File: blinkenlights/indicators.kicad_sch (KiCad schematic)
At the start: 50 parts, among them U401 74HC244, U402 74AUC2G34

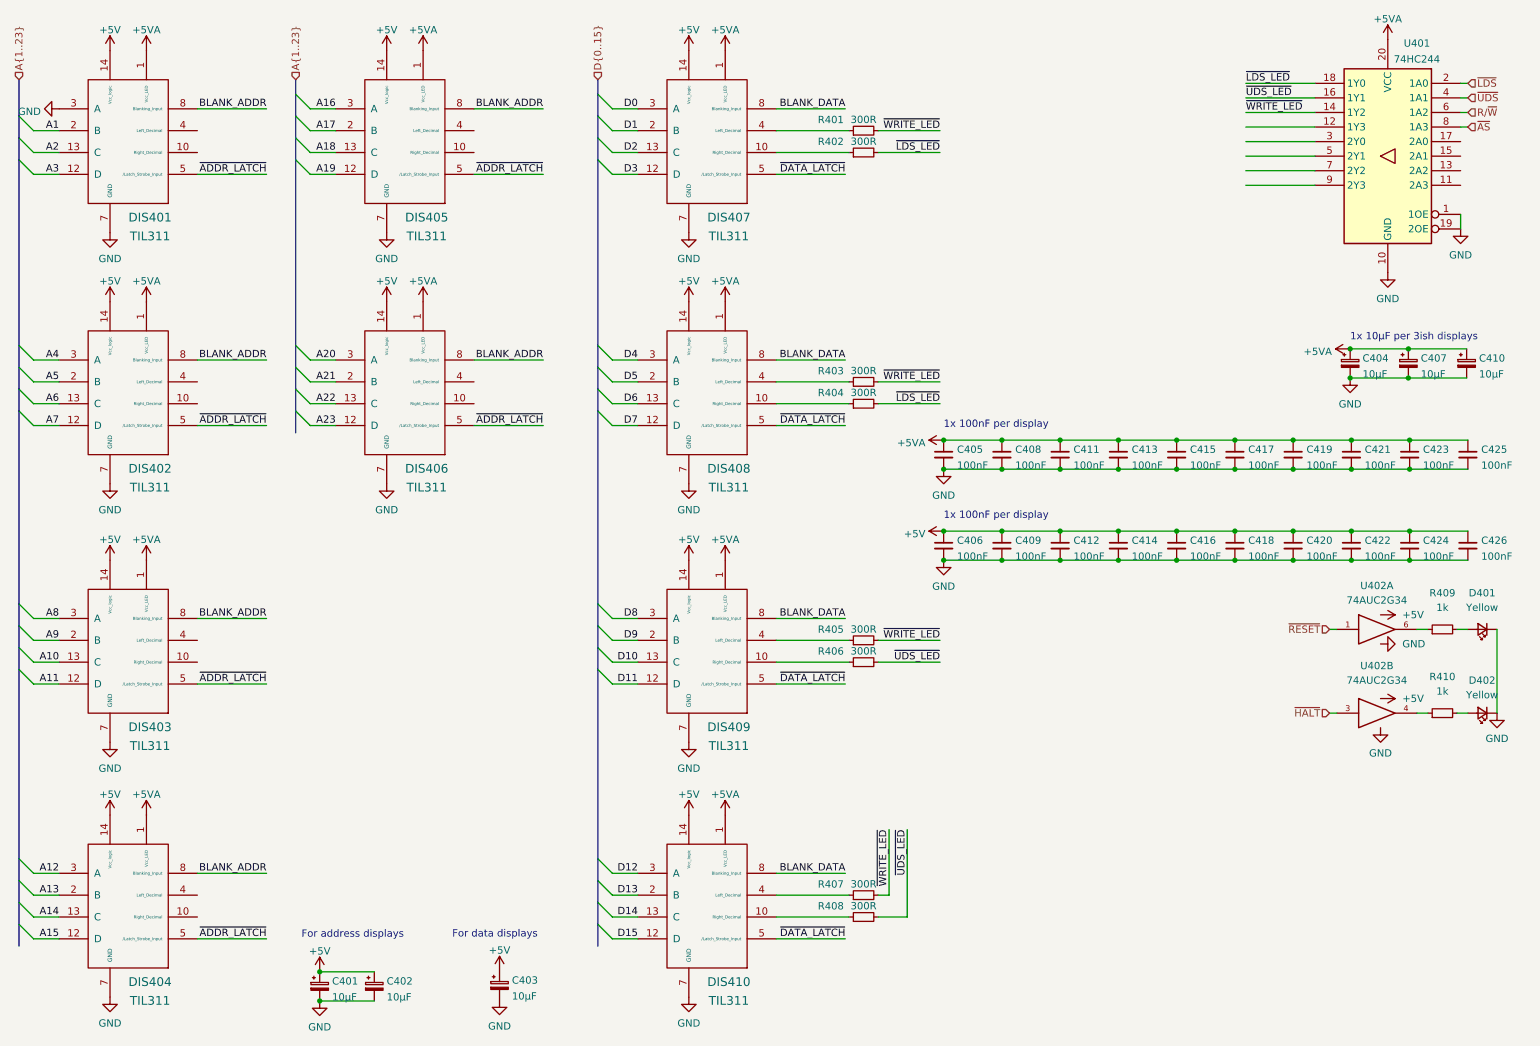
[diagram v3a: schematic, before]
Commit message: Routed address/data bus on blinkenlights
- It goes to the funky hex display bois now and is routed so that it
  should be pretty ez to yeet on down into level shifters for the big
  ARM chip that runs the show
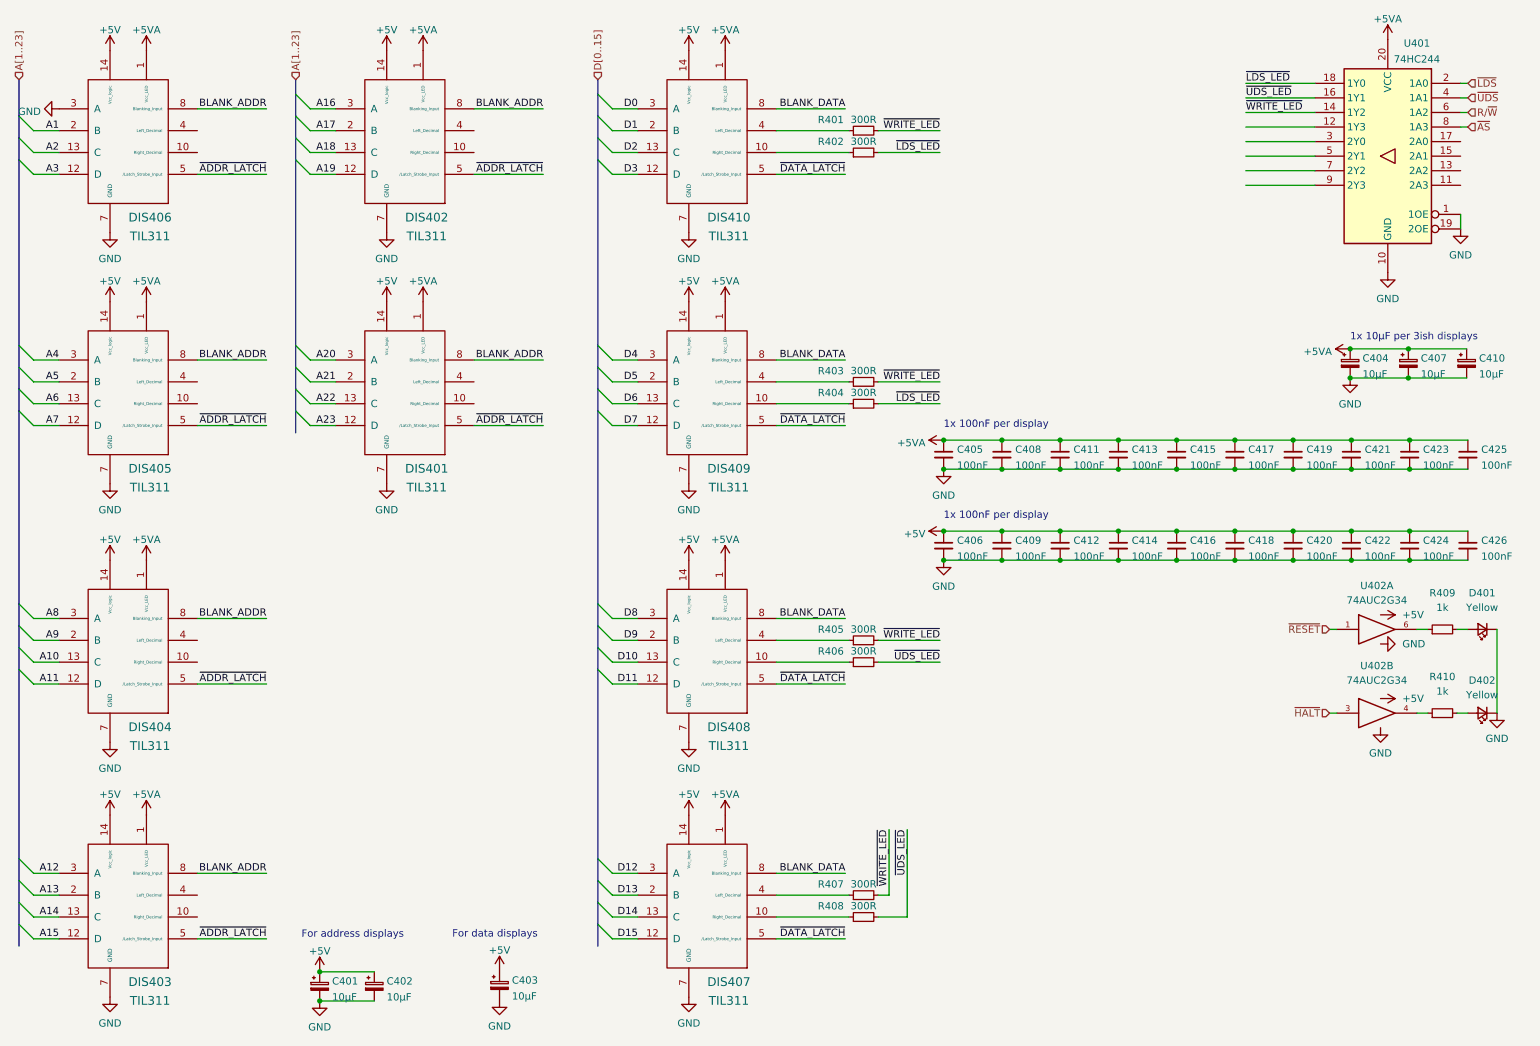
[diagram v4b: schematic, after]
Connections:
- net A1: now also DIS406.2 (B); no longer DIS401.2 (B)
- net A10: now also DIS404.13 (C); no longer DIS403.13 (C)
- net A11: now also DIS404.12 (D); no longer DIS403.12 (D)
- net A12: now also DIS403.3 (A); no longer DIS404.3 (A)
- net A13: now also DIS403.2 (B); no longer DIS404.2 (B)
- net A14: now also DIS403.13 (C); no longer DIS404.13 (C)
- net A15: now also DIS403.12 (D); no longer DIS404.12 (D)
- net A16: now also DIS402.3 (A); no longer DIS405.3 (A)
- net A17: now also DIS402.2 (B); no longer DIS405.2 (B)
- net A18: now also DIS402.13 (C); no longer DIS405.13 (C)
- net A19: now also DIS402.12 (D); no longer DIS405.12 (D)
- net A2: now also DIS406.13 (C); no longer DIS401.13 (C)
- net A20: now also DIS401.3 (A); no longer DIS406.3 (A)
- net A21: now also DIS401.2 (B); no longer DIS406.2 (B)
- net A22: now also DIS401.13 (C); no longer DIS406.13 (C)
- net A23: now also DIS401.12 (D); no longer DIS406.12 (D)
- net A3: now also DIS406.12 (D); no longer DIS401.12 (D)
- net A4: now also DIS405.3 (A); no longer DIS402.3 (A)
- net A5: now also DIS405.2 (B); no longer DIS402.2 (B)
- net A6: now also DIS405.13 (C); no longer DIS402.13 (C)
- net A7: now also DIS405.12 (D); no longer DIS402.12 (D)
- net A8: now also DIS404.3 (A); no longer DIS403.3 (A)
- net A9: now also DIS404.2 (B); no longer DIS403.2 (B)
- net D0: now also DIS410.3 (A); no longer DIS407.3 (A)
- net D1: now also DIS410.2 (B); no longer DIS407.2 (B)
- net D10: now also DIS408.13 (C); no longer DIS409.13 (C)
- net D11: now also DIS408.12 (D); no longer DIS409.12 (D)
- net D12: now also DIS407.3 (A); no longer DIS410.3 (A)
- net D13: now also DIS407.2 (B); no longer DIS410.2 (B)
- net D14: now also DIS407.13 (C); no longer DIS410.13 (C)
- net D15: now also DIS407.12 (D); no longer DIS410.12 (D)
- net D2: now also DIS410.13 (C); no longer DIS407.13 (C)
- net D3: now also DIS410.12 (D); no longer DIS407.12 (D)
- net D4: now also DIS409.3 (A); no longer DIS408.3 (A)
- net D5: now also DIS409.2 (B); no longer DIS408.2 (B)
- net D6: now also DIS409.13 (C); no longer DIS408.13 (C)
- net D7: now also DIS409.12 (D); no longer DIS408.12 (D)
- net D8: now also DIS408.3 (A); no longer DIS409.3 (A)
- net D9: now also DIS408.2 (B); no longer DIS409.2 (B)
- net GND: now also DIS406.3 (A); no longer DIS401.3 (A)
- net at DIS407.10 (Right_Decimal): now also R408.1; no longer R402.1
- net at DIS407.4 (Left_Decimal): now also R407.1; no longer R401.1
- net at DIS410.4 (Left_Decimal): now also R401.1; no longer R407.1
- net at DIS410.10 (Right_Decimal): now also R402.1; no longer R408.1
- net at R406.1: now also DIS408.10 (Right_Decimal); no longer DIS409.10 (Right_Decimal)
- net at R403.1: now also DIS409.4 (Left_Decimal); no longer DIS408.4 (Left_Decimal)
- net at R405.1: now also DIS408.4 (Left_Decimal); no longer DIS409.4 (Left_Decimal)
- net at R404.1: now also DIS409.10 (Right_Decimal); no longer DIS408.10 (Right_Decimal)
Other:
- moved on the sheet: DIS401, DIS402, DIS403, DIS404, DIS405, DIS406, DIS407, DIS408, DIS409, DIS410

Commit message: Routed control signals
- The blinkenlights board now has the control signals routed to IO
  expanders, and removed a bunch of superfluous level shifting type
  stuff
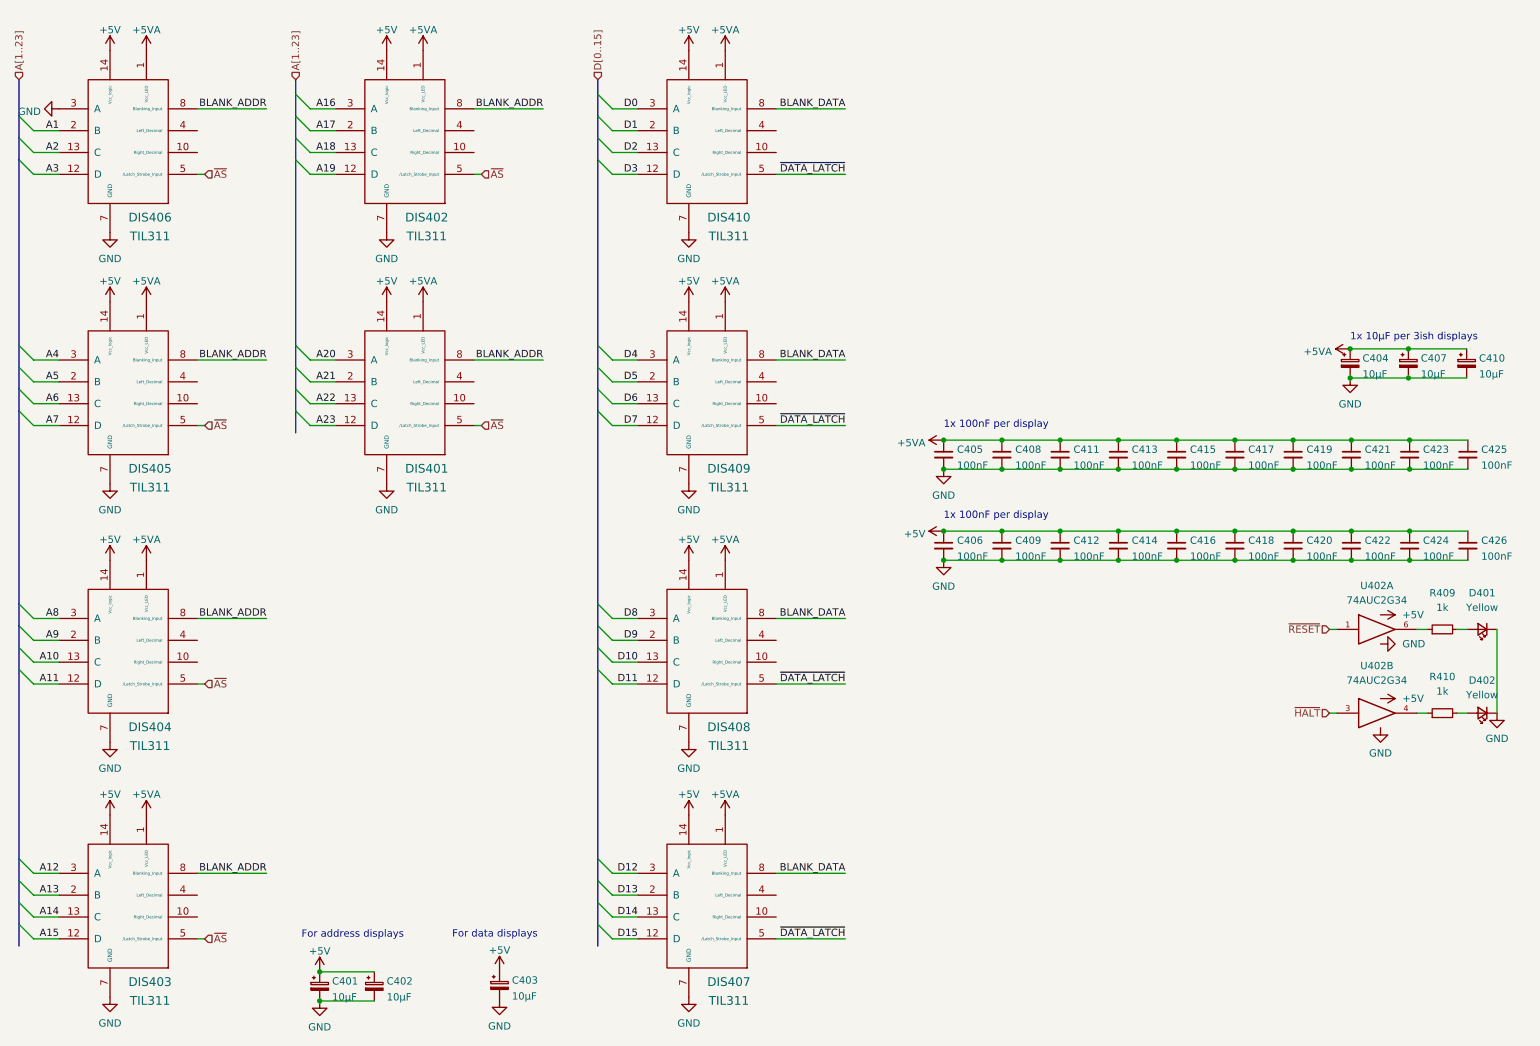
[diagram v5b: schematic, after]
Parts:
- removed R401, R402, R403, R404, R405, R406, R407, R408: 300R, Resistor_SMD:R_0805_2012Metric, symbol Device:R_Small
- removed U401: 74HC244, Package_SO:TSSOP-20_4.4x6.5mm_P0.65mm, symbol 74xx:74HC244
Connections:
- net ~{ADDR_LATCH} is gone; now on net ~{AS}: DIS401.5 (/Latch_Strobe_Input), DIS402.5 (/Latch_Strobe_Input), DIS403.5 (/Latch_Strobe_Input), DIS404.5 (/Latch_Strobe_Input), DIS405.5 (/Latch_Strobe_Input), DIS406.5 (/Latch_Strobe_Input)

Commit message: Finish routing of blinkenlights board
- Completed routing of the board, including the function code lines and
  other such fun stuff
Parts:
- U402: footprint Package_TO_SOT_SMD:SOT-23-6 -> Package_TO_SOT_SMD:SOT-23-6_Handsoldering
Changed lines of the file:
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@@
     (property "Reference" "U402" (id 0) (at 257.175 115.57 0))
     (property "Value" "74AUC2G34" (id 1) (at 257.175 118.11 0))
-    (property "Footprint" "Package_TO_SOT_SMD:SOT-23-6" (id 2) (at 257.81 123.19 0)
+    (property "Footprint" "Package_TO_SOT_SMD:SOT-23-6_Handsoldering" (id 2) (at 257.81 123.19 0)
       (effects (font (size 1.27 1.27)) hide)
     )
@@
     (property "Reference" "U402" (id 0) (at 257.175 129.54 0))
     (property "Value" "74AUC2G34" (id 1) (at 257.175 132.08 0))
-    (property "Footprint" "Package_TO_SOT_SMD:SOT-23-6" (id 2) (at 257.81 137.795 0)
-      (effects (font (size 1.27 1.27)) hide)
-    )
+    (property "Footprint" "Package_TO_SOT_SMD:SOT-23-6_Handsoldering" (id 2) (at 257.81 137.795 0)
+      (effects (font (size 1.27 1.27)) hide)
+    )

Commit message: Added a few more test points
- Also, tweaked the package of the I2C translator to be one that's
  actually in stock
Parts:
- added R401, R402: 0R, Resistor_SMD:R_0805_2012Metric, symbol Device:R_Small
- U402: value 74AUC2G34 -> 74LVC2G34; footprint Package_TO_SOT_SMD:SOT-23-6_Handsoldering -> Package_TO_SOT_SMD:SOT-363_SC-70-6_Handsoldering; symbol 74xGxx:74AUC2G34 -> 74xGxx:74LVC2G34; MPN SN74AUC2G34DBVR -> 74LVC2G34DW-7
- U402: value 74AUC2G34 -> 74LVC2G34
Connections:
- net BLANK_ADDR: now also R401.2
- net BLANK_DATA: now also R402.2
- net GND: now also R401.1, R402.1
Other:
- note added: "Do not blank the displays, ever"
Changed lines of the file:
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@@
 (kicad_sch (version 20211123) (generator eeschema)
   (paper "A4")
+  (junction (at 86.36 130.175) (diameter 0) (color 0 0 0 0)
+  )
   (junction (at 262.89 111.125) (diameter 0) (color 0 0 0 0)
   )
@@
     (stroke (width 0) (type default) (color 0 0 0 0))
   )
+  (wire (pts (xy 91.44 130.175) (xy 103.505 130.175))
+    (stroke (width 0) (type default) (color 0 0 0 0))
+  )
   (wire (pts (xy 22.86 87.63) (xy 27.305 87.63))
     (stroke (width 0) (type default) (color 0 0 0 0))
@@
     (stroke (width 0) (type default) (color 0 0 0 0))
   )
+  (wire (pts (xy 86.36 121.285) (xy 86.36 130.175))
+    (stroke (width 0) (type default) (color 0 0 0 0))
+  )
   (wire (pts (xy 123.825 125.095) (xy 128.27 125.095))
     (stroke (width 0) (type default) (color 0 0 0 0))
@@
   )
   (bus (pts (xy 20.32 163.195) (xy 20.32 167.005))
+    (stroke (width 0) (type default) (color 0 0 0 0))
+  )
+  (wire (pts (xy 91.44 121.285) (xy 103.505 121.285))
     (stroke (width 0) (type default) (color 0 0 0 0))
   )
@@
     (effects (font (size 1.27 1.27)) (justify left bottom))
   )
+  (text "Do not blank the displays, ever" (at 83.185 113.665 0)
+    (effects (font (size 1.27 1.27)) (justify left bottom))
+  )
   (label "~{DATA_LATCH}" (at 164.465 43.815 180)
     (effects (font (size 1.27 1.27)) (justify right bottom))
@@
     (effects (font (size 1.27 1.27)) (justify right bottom))
   )
+  (label "BLANK_ADDR" (at 103.505 121.285 180)
+    (effects (font (size 1.27 1.27)) (justify right bottom))
+  )
   (label "D2" (at 128.27 40.005 180)
     (effects (font (size 1.27 1.27)) (justify right bottom))
@@
   )
   (label "A17" (at 75.565 36.195 180)
+    (effects (font (size 1.27 1.27)) (justify right bottom))
+  )
+  (label "BLANK_DATA" (at 103.505 130.175 180)
     (effects (font (size 1.27 1.27)) (justify right bottom))
   )
@@
     (pin "2")
   )
-  (symbol (lib_id "74xGxx:74AUC2G34") (at 257.81 123.19 0) (unit 1)
+  (symbol (lib_id "74xGxx:74LVC2G34") (at 257.81 123.19 0) (unit 1)
     (in_bom yes) (on_board yes) (fields_autoplaced)
     (property "Reference" "U402" (id 0) (at 257.175 115.57 0))
-    (property "Value" "74AUC2G34" (id 1) (at 257.175 118.11 0))
-    (property "Footprint" "Package_TO_SOT_SMD:SOT-23-6_Handsoldering" (id 2) (at 257.81 123.19 0)
+    (property "Value" "74LVC2G34" (id 1) (at 257.175 118.11 0))
+    (property "Footprint" "Package_TO_SOT_SMD:SOT-363_SC-70-6_Handsoldering" (id 2) (at 257.81 123.19 0)
       (effects (font (size 1.27 1.27)) hide)
     )
@@
       (effects (font (size 1.27 1.27)) hide)
     )
-    (property "MPN" "SN74AUC2G34DBVR" (id 4) (at 257.81 123.19 0)
+    (property "MPN" "74LVC2G34DW-7" (id 4) (at 257.81 123.19 0)
       (effects (font (size 1.27 1.27)) hide)
     )
@@
     (pin "1")
   )
+  (symbol (lib_id "Device:R_Small") (at 88.9 130.175 90) (unit 1)
+    (in_bom yes) (on_board yes) (fields_autoplaced)
+    (property "Reference" "R402" (id 0) (at 88.9 124.46 90))
+    (property "Value" "0R" (id 1) (at 88.9 127 90))
+    (property "Footprint" "Resistor_SMD:R_0805_2012Metric" (id 2) (at 88.9 130.175 0)
+      (effects (font (size 1.27 1.27)) hide)
+    )
+    (property "Datasheet" "~" (id 3) (at 88.9 130.175 0)
+      (effects (font (size 1.27 1.27)) hide)
+    )
+    (property "MPN" "RC0805JR-100RL" (id 4) (at 88.9 130.175 90)
+      (effects (font (size 1.27 1.27)) hide)
+    )
+    (pin "1")
+    (pin "2")
+  )
   (symbol (lib_id "Device:C_Small") (at 262.89 108.585 0) (unit 1)
     (in_bom yes) (on_board yes)
@@
     (pin "1")
   )
+  (symbol (lib_id "Device:R_Small") (at 88.9 121.285 90) (unit 1)
+    (in_bom yes) (on_board yes) (fields_autoplaced)
+    (property "Reference" "R401" (id 0) (at 88.9 115.57 90))
+    (property "Value" "0R" (id 1) (at 88.9 118.11 90))
+    (property "Footprint" "Resistor_SMD:R_0805_2012Metric" (id 2) (at 88.9 121.285 0)
+      (effects (font (size 1.27 1.27)) hide)
+    )
+    (property "Datasheet" "~" (id 3) (at 88.9 121.285 0)
+      (effects (font (size 1.27 1.27)) hide)
+    )
+    (property "MPN" "RC0805JR-100RL" (id 4) (at 88.9 121.285 90)
+      (effects (font (size 1.27 1.27)) hide)
+    )
+    (pin "1")
+    (pin "2")
+  )
+  (symbol (lib_id "power:GND") (at 86.36 130.175 0) (unit 1)
+    (in_bom yes) (on_board yes) (fields_autoplaced)
+    (property "Reference" "#PWR0443" (id 0) (at 86.36 136.525 0)
+      (effects (font (size 1.27 1.27)) hide)
+    )
+    (property "Value" "GND" (id 1) (at 86.36 134.62 0))
+    (property "Footprint" "" (id 2) (at 86.36 130.175 0)
+      (effects (font (size 1.27 1.27)) hide)
+    )
+    (property "Datasheet" "" (id 3) (at 86.36 130.175 0)
+      (effects (font (size 1.27 1.27)) hide)
+    )
+    (pin "1")
+  )
   (symbol (lib_id "power:GND") (at 278.13 137.795 0) (unit 1)
     (in_bom yes) (on_board yes) (fields_autoplaced)
@@
     (in_bom yes) (on_board yes) (fields_autoplaced)
     (property "Reference" "U402" (id 0) (at 257.175 129.54 0))
-    (property "Value" "74AUC2G34" (id 1) (at 257.175 132.08 0))
+    (property "Value" "74LVC2G34" (id 1) (at 257.175 132.08 0))
     (property "Footprint" "Package_TO_SOT_SMD:SOT-23-6_Handsoldering" (id 2) (at 257.81 137.795 0)
       (effects (font (size 1.27 1.27)) hide)
